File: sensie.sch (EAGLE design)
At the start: 26 parts, among them J2 BATT, Q1 MOSFET-PCHANNELSMD, Q2 MOSFET-NCHANNELBSS138, Q3 20MHz

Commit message: Routing cleanup 3.
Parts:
- removed JP1: USB-MICROB, SparkFun-Connectors:USB-MICROB
- added JP3: USB-MICROB, bafoontecha:USB-MICROB
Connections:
- removed net N$3: J2-2.S
- net GND: now also J2-2.S, JP3.GND; no longer JP1.GND
- net N$14: now also JP3.D+; no longer JP1.D+
- net N$15: now also JP3.D-; no longer JP1.D-
- net VIN_USB: now also JP3.VBUS; no longer JP1.VBUS
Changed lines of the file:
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@@
 <part name="GND7" library="supply1" deviceset="GND" device=""/>
 <part name="GND9" library="supply1" deviceset="GND" device=""/>
-<part name="JP1" library="SparkFun-Connectors" deviceset="USB" device="-MICROB"/>
 <part name="GND11" library="supply1" deviceset="GND" device=""/>
 <part name="Q2" library="SparkFun-DiscreteSemi" deviceset="MOSFET-NCHANNEL" device="BSS138"/>
 <part name="GND12" library="supply1" deviceset="GND" device=""/>
 <part name="JP2" library="SparkFun-Connectors" deviceset="M07" device=""/>
+<part name="JP3" library="bafoontecha" deviceset="USB" device="-MICROB"/>
 </parts>
 <sheets>
@@
 <instance part="GND7" gate="1" x="53.34" y="35.56"/>
 <instance part="GND9" gate="1" x="177.546" y="147.32"/>
-<instance part="JP1" gate="G$1" x="182.626" y="153.67"/>
 <instance part="GND11" gate="1" x="358.14" y="53.34"/>
 <instance part="Q2" gate="G$1" x="332.74" y="45.72"/>
 <instance part="GND12" gate="1" x="332.74" y="35.56"/>
 <instance part="JP2" gate="G$1" x="279.4" y="38.1" rot="R180"/>
+<instance part="JP3" gate="G$1" x="183.134" y="153.67"/>
 </instances>
 <busses>
@@
 <wire x1="274.32" y1="63.5" x2="264.16" y2="63.5" width="0.1524" layer="91"/>
 <label x="264.16" y="63.5" size="1.778" layer="95"/>
+<junction x="274.32" y="63.5"/>
 </segment>
 <segment>
@@
 <wire x1="53.34" y1="43.18" x2="58.42" y2="43.18" width="0.1524" layer="91"/>
 <wire x1="53.34" y1="38.1" x2="53.34" y2="43.18" width="0.1524" layer="91"/>
-</segment>
-<segment>
-<pinref part="JP1" gate="G$1" pin="GND"/>
+<junction x="53.34" y="43.18"/>
+</segment>
+<segment>
 <pinref part="GND9" gate="1" pin="GND"/>
-<wire x1="180.086" y1="153.67" x2="177.546" y2="153.67" width="0.1524" layer="91"/>
+<wire x1="180.594" y1="153.67" x2="177.546" y2="153.67" width="0.1524" layer="91"/>
 <wire x1="177.546" y1="153.67" x2="177.546" y2="149.86" width="0.1524" layer="91"/>
+<pinref part="JP3" gate="G$1" pin="GND"/>
+<junction x="180.594" y="153.67"/>
 </segment>
 <segment>
@@
 <pinref part="GND11" gate="1" pin="GND"/>
 <wire x1="358.14" y1="58.42" x2="358.14" y2="55.88" width="0.1524" layer="91"/>
+<junction x="358.14" y="58.42"/>
+<junction x="358.14" y="60.96"/>
+<junction x="358.14" y="63.5"/>
+<junction x="358.14" y="66.04"/>
+<junction x="358.14" y="71.12"/>
+<junction x="358.14" y="68.58"/>
+<junction x="358.14" y="73.66"/>
 </segment>
 <segment>
@@
 <pinref part="GND12" gate="1" pin="GND"/>
 <wire x1="332.74" y1="40.64" x2="332.74" y2="38.1" width="0.1524" layer="91"/>
+<junction x="332.74" y="40.64"/>
+<junction x="332.74" y="38.1"/>
 </segment>
 <segment>
@@
 <wire x1="312.42" y1="106.68" x2="312.42" y2="104.14" width="0.1524" layer="91"/>
 <wire x1="312.42" y1="104.14" x2="314.96" y2="104.14" width="0.1524" layer="91"/>
+<junction x="314.96" y="104.14"/>
+<junction x="312.42" y="106.68"/>
 </segment>
 <segment>
@@
 <wire x1="274.32" y1="76.2" x2="264.16" y2="76.2" width="0.1524" layer="91"/>
 <label x="264.16" y="76.2" size="1.778" layer="95"/>
+<junction x="274.32" y="76.2"/>
+</segment>
+<segment>
+<pinref part="J2" gate="-2" pin="S"/>
+<wire x1="287.02" y1="223.52" x2="287.02" y2="222.25" width="0.1524" layer="91"/>
+<junction x="287.02" y="223.52"/>
+<pinref part="GND2" gate="1" pin="GND"/>
+<junction x="287.02" y="222.25"/>
+<wire x1="287.02" y1="222.25" x2="287.02" y2="221.996" width="0.1524" layer="91"/>
 </segment>
 </net>
@@
 </segment>
 <segment>
-<wire x1="180.086" y1="156.21" x2="170.942" y2="156.21" width="0.1524" layer="91"/>
+<wire x1="180.594" y1="156.21" x2="170.942" y2="156.21" width="0.1524" layer="91"/>
 <label x="162.56" y="156.464" size="1.778" layer="95"/>
-<pinref part="JP1" gate="G$1" pin="VBUS"/>
+<pinref part="JP3" gate="G$1" pin="VBUS"/>
+<junction x="180.594" y="156.21"/>
 </segment>
 </net>
@@
 <net name="N$14" class="0">
 <segment>
-<wire x1="143.51" y1="161.29" x2="180.086" y2="161.29" width="0.1524" layer="91"/>
+<wire x1="143.51" y1="161.29" x2="180.594" y2="161.29" width="0.1524" layer="91"/>
 <pinref part="U$3" gate="G$1" pin="RC5/D+"/>
-<pinref part="JP1" gate="G$1" pin="D+"/>
+<pinref part="JP3" gate="G$1" pin="D+"/>
+<junction x="180.594" y="161.29"/>
 </segment>
 </net>
 <net name="N$15" class="0">
 <segment>
-<wire x1="180.086" y1="158.75" x2="143.51" y2="158.75" width="0.1524" layer="91"/>
+<wire x1="180.594" y1="158.75" x2="143.51" y2="158.75" width="0.1524" layer="91"/>
 <pinref part="U$3" gate="G$1" pin="RC4/D-"/>
-<pinref part="JP1" gate="G$1" pin="D-"/>
+<pinref part="JP3" gate="G$1" pin="D-"/>
+<junction x="180.594" y="158.75"/>
 </segment>
 </net>
@@
 <pinref part="IC1" gate="G$1" pin="OUT"/>
 <wire x1="359.41" y1="210.82" x2="375.92" y2="210.82" width="0.1524" layer="91"/>
+<junction x="375.92" y="210.82"/>
 </segment>
 <segment>
@@
 <wire x1="330.2" y1="104.14" x2="335.28" y2="104.14" width="0.1524" layer="91"/>
 <label x="332.74" y="104.14" size="1.778" layer="95"/>
+<junction x="330.2" y="104.14"/>
 </segment>
 <segment>
@@
 <label x="264.16" y="66.04" size="1.778" layer="95"/>
 <label x="264.16" y="66.04" size="1.778" layer="95"/>
+<junction x="274.32" y="66.04"/>
 </segment>
 <segment>
@@
 <pinref part="Q2" gate="G$1" pin="D"/>
 <wire x1="332.74" y1="58.42" x2="332.74" y2="50.8" width="0.1524" layer="91"/>
+<junction x="332.74" y="58.42"/>
+<junction x="332.74" y="60.96"/>
+<junction x="332.74" y="63.5"/>
+<junction x="332.74" y="66.04"/>
+<junction x="332.74" y="68.58"/>
+<junction x="332.74" y="71.12"/>
+<junction x="332.74" y="73.66"/>
+<junction x="332.74" y="50.8"/>
 </segment>
 <segment>
@@
 <wire x1="274.32" y1="88.9" x2="264.16" y2="88.9" width="0.1524" layer="91"/>
 <label x="264.16" y="88.9" size="1.778" layer="95"/>
+<junction x="274.32" y="88.9"/>
 </segment>
 </net>
@@
 <label x="264.16" y="40.64" size="1.778" layer="95"/>
 <pinref part="JP2" gate="G$1" pin="2"/>
+<junction x="274.32" y="40.64"/>
 </segment>
 </net>
@@
 <label x="264.16" y="38.1" size="1.778" layer="95"/>
 <pinref part="JP2" gate="G$1" pin="3"/>
+<junction x="274.32" y="38.1"/>
 </segment>
 </net>
@@
 <label x="264.16" y="35.56" size="1.778" layer="95"/>
 <pinref part="JP2" gate="G$1" pin="4"/>
+<junction x="274.32" y="35.56"/>
 </segment>
 </net>
@@
 <label x="264.16" y="33.02" size="1.778" layer="95"/>
 <pinref part="JP2" gate="G$1" pin="5"/>
-</segment>
-</net>
-<net name="N$3" class="0">
-<segment>
-<pinref part="J2" gate="-2" pin="S"/>
-<wire x1="287.02" y1="223.52" x2="287.02" y2="221.996" width="0.1524" layer="91"/>
+<junction x="274.32" y="33.02"/>
 </segment>
 </net>
@@
 <wire x1="330.2" y1="101.6" x2="335.28" y2="101.6" width="0.1524" layer="91"/>
 <label x="332.74" y="101.6" size="1.778" layer="95"/>
+<junction x="330.2" y="101.6"/>
 </segment>
 <segment>
@@
 <wire x1="330.2" y1="99.06" x2="335.28" y2="99.06" width="0.1524" layer="91"/>
 <label x="332.74" y="99.06" size="1.778" layer="95"/>
+<junction x="330.2" y="99.06"/>
 </segment>
 <segment>
@@
 <wire x1="274.32" y1="60.96" x2="264.16" y2="60.96" width="0.1524" layer="91"/>
 <label x="254" y="60.96" size="1.778" layer="95"/>
+<junction x="274.32" y="60.96"/>
 </segment>
 </net>
@@
 <wire x1="330.2" y1="96.52" x2="335.28" y2="96.52" width="0.1524" layer="91"/>
 <label x="332.74" y="96.52" size="1.778" layer="95"/>
+<junction x="330.2" y="96.52"/>
 </segment>
 <segment>
@@
 <wire x1="314.96" y1="101.6" x2="310.642" y2="101.6" width="0.1524" layer="91"/>
 <label x="298.45" y="101.854" size="1.778" layer="95"/>
+<junction x="314.96" y="101.6"/>
 </segment>
 <segment>
@@
 <wire x1="314.96" y1="99.06" x2="310.642" y2="99.06" width="0.1524" layer="91"/>
 <label x="298.45" y="99.314" size="1.778" layer="95"/>
+<junction x="314.96" y="99.06"/>
 </segment>
 <segment>
@@
 <wire x1="274.32" y1="81.28" x2="264.16" y2="81.28" width="0.1524" layer="91"/>
 <label x="264.16" y="81.28" size="1.778" layer="95"/>
+<junction x="274.32" y="81.28"/>
 </segment>
 </net>
@@
 <wire x1="314.96" y1="96.52" x2="310.642" y2="96.52" width="0.1524" layer="91"/>
 <label x="298.45" y="96.774" size="1.778" layer="95"/>
+<junction x="314.96" y="96.52"/>
 </segment>
 <segment>
@@
 <wire x1="274.32" y1="78.74" x2="264.16" y2="78.74" width="0.1524" layer="91"/>
 <label x="264.16" y="78.74" size="1.778" layer="95"/>
+<junction x="274.32" y="78.74"/>
 </segment>
 </net>
@@
 <wire x1="274.32" y1="83.82" x2="264.16" y2="83.82" width="0.1524" layer="91"/>
 <label x="264.16" y="83.82" size="1.778" layer="95"/>
+<junction x="274.32" y="83.82"/>
 </segment>
 </net>
@@
 <wire x1="274.32" y1="86.36" x2="264.16" y2="86.36" width="0.1524" layer="91"/>
 <label x="264.16" y="86.36" size="1.778" layer="95"/>
+<junction x="274.32" y="86.36"/>
 </segment>
 </net>
@@
 <wire x1="325.12" y1="45.72" x2="317.5" y2="45.72" width="0.1524" layer="91"/>
 <label x="306.832" y="45.72" size="1.778" layer="95"/>
+<junction x="325.12" y="45.72"/>
 </segment>
 </net>
@@
 <label x="264.16" y="30.48" size="1.778" layer="95"/>
 <pinref part="JP2" gate="G$1" pin="6"/>
+<junction x="274.32" y="30.48"/>
 </segment>
 </net>
@@
 <label x="264.16" y="27.94" size="1.778" layer="95"/>
 <pinref part="JP2" gate="G$1" pin="7"/>
+<junction x="274.32" y="27.94"/>
 </segment>
 </net>
@@
 <wire x1="274.32" y1="58.42" x2="264.16" y2="58.42" width="0.1524" layer="91"/>
 <label x="254" y="58.42" size="1.778" layer="95"/>
+<junction x="274.32" y="58.42"/>
 </segment>
 <segment>
@@
 <pinref part="R1" gate="G$1" pin="1"/>
 <wire x1="58.42" y1="55.88" x2="58.42" y2="63.5" width="0.1524" layer="91"/>
+<junction x="58.42" y="55.88"/>
 </segment>
 </net>
@@
 <wire x1="48.26" y1="55.88" x2="48.26" y2="76.2" width="0.1524" layer="91"/>
 <label x="48.26" y="76.2" size="1.778" layer="95"/>
+<junction x="48.26" y="55.88"/>
 </segment>
 <segment>
@@
 <wire x1="274.32" y1="43.18" x2="263.906" y2="43.18" width="0.1524" layer="91"/>
 <label x="264.16" y="43.18" size="1.778" layer="95"/>
-</segment>
-<segment>
+<junction x="274.32" y="43.18"/>
+</segment>
+<segment>

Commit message: About to do ground pours.
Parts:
- removed R13: 10k, SparkFun:RESISTOR
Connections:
- net 3.3V: now also SENSOR.6; no longer R13.2, SENSOR.1
- net GND: now also SENSOR.1; no longer SENSOR.6
- net VPP: no longer R13.1
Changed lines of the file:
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@@
 <part name="C6" library="SparkFun" deviceset="CAP" device="SMD" value="10uF"/>
 <part name="GND19" library="SparkFun" deviceset="GND" device=""/>
-<part name="GND24" library="SparkFun" deviceset="GND" device=""/>
-<part name="R13" library="SparkFun" deviceset="RESISTOR" device="" value="10k"/>
-<part name="P+4" library="SparkFun" deviceset="3.3V" device=""/>
 <part name="GND2" library="SparkFun" deviceset="GND" device=""/>
 <part name="GND3" library="supply1" deviceset="GND" device=""/>
@@
 <instance part="C6" gate="G$1" x="375.92" y="203.2"/>
 <instance part="GND19" gate="1" x="375.92" y="198.12"/>
-<instance part="GND24" gate="1" x="58.42" y="205.74"/>
-<instance part="R13" gate="G$1" x="58.42" y="226.06" rot="R90"/>
-<instance part="P+4" gate="G$1" x="58.42" y="231.14"/>
 <instance part="GND2" gate="1" x="287.02" y="219.71"/>
 <instance part="GND3" gate="1" x="312.42" y="109.22" rot="R180"/>
@@
 </segment>
 <segment>
-<wire x1="213.36" y1="182.88" x2="205.74" y2="182.88" width="0.1524" layer="91"/>
+<wire x1="217.17" y1="182.88" x2="205.74" y2="182.88" width="0.1524" layer="91"/>
 <label x="205.74" y="182.88" size="1.778" layer="95"/>
 </segment>
@@
 </segment>
 <segment>
-<pinref part="SENSOR" gate="G$1" pin="6"/>
-<wire x1="274.32" y1="76.2" x2="264.16" y2="76.2" width="0.1524" layer="91"/>
-<label x="264.16" y="76.2" size="1.778" layer="95"/>
-<junction x="274.32" y="76.2"/>
-</segment>
-<segment>
 <pinref part="J2" gate="-2" pin="S"/>
 <wire x1="287.02" y1="223.52" x2="287.02" y2="222.25" width="0.1524" layer="91"/>
@@
 <junction x="287.02" y="222.25"/>
 <wire x1="287.02" y1="222.25" x2="287.02" y2="221.996" width="0.1524" layer="91"/>
+</segment>
+<segment>
+<pinref part="SENSOR" gate="G$1" pin="1"/>
+<wire x1="274.32" y1="88.9" x2="264.16" y2="88.9" width="0.1524" layer="91"/>
+<label x="264.16" y="88.9" size="1.778" layer="95"/>
+<junction x="274.32" y="88.9"/>
 </segment>
 </net>
@@
 <net name="VPP" class="0">
 <segment>
-<wire x1="213.36" y1="177.8" x2="205.74" y2="177.8" width="0.1524" layer="91"/>
+<wire x1="217.17" y1="177.8" x2="205.74" y2="177.8" width="0.1524" layer="91"/>
 <label x="205.74" y="177.8" size="1.778" layer="95"/>
 </segment>
@@
 <label x="90.17" y="191.77" size="1.778" layer="95"/>
 <pinref part="U$3" gate="G$1" pin="MCLR/VPP"/>
-</segment>
-<segment>
-<wire x1="58.42" y1="220.98" x2="58.42" y2="219.71" width="0.1524" layer="91"/>
-<wire x1="58.42" y1="219.71" x2="58.42" y2="218.44" width="0.1524" layer="91"/>
-<wire x1="58.42" y1="219.71" x2="66.04" y2="219.71" width="0.1524" layer="91"/>
-<junction x="58.42" y="219.71"/>
-<label x="60.96" y="219.71" size="1.778" layer="95"/>
-<pinref part="R13" gate="G$1" pin="1"/>
 </segment>
 </net>
@@
 </segment>
 <segment>
-<wire x1="213.36" y1="180.34" x2="205.74" y2="180.34" width="0.1524" layer="91"/>
+<wire x1="217.17" y1="180.34" x2="205.74" y2="180.34" width="0.1524" layer="91"/>
 <label x="205.74" y="180.34" size="1.778" layer="95"/>
-</segment>
-<segment>
-<pinref part="R13" gate="G$1" pin="2"/>
-<pinref part="P+4" gate="G$1" pin="3.3V"/>
 </segment>
 <segment>
@@
 </segment>
 <segment>
-<pinref part="SENSOR" gate="G$1" pin="1"/>
-<wire x1="274.32" y1="88.9" x2="264.16" y2="88.9" width="0.1524" layer="91"/>
-<label x="264.16" y="88.9" size="1.778" layer="95"/>
-<junction x="274.32" y="88.9"/>
+<pinref part="SENSOR" gate="G$1" pin="6"/>
+<wire x1="274.32" y1="76.2" x2="264.16" y2="76.2" width="0.1524" layer="91"/>
+<label x="264.16" y="76.2" size="1.778" layer="95"/>
+<junction x="274.32" y="76.2"/>
 </segment>
 </net>
@@
 </segment>
 </net>
-<net name="LCD_DB5" class="0">
-<segment>
-<wire x1="213.36" y1="190.5" x2="205.74" y2="190.5" width="0.1524" layer="91"/>
-<label x="205.74" y="190.5" size="1.778" layer="95"/>
-</segment>
-</net>
-<net name="LCD_DB6" class="0">
-<segment>
-<wire x1="213.36" y1="187.96" x2="205.74" y2="187.96" width="0.1524" layer="91"/>
-<label x="205.74" y="187.96" size="1.778" layer="95"/>
-</segment>
-</net>
-<net name="LCD_DB7" class="0">
-<segment>
-<wire x1="213.36" y1="185.42" x2="205.74" y2="185.42" width="0.1524" layer="91"/>
-<label x="205.74" y="185.42" size="1.778" layer="95"/>
-</segment>
-</net>
 <net name="AN3" class="0">
 <segment>
@@
 <junction x="274.32" y="83.82"/>
 </segment>
+<segment>
+<wire x1="217.17" y1="190.5" x2="205.74" y2="190.5" width="0.1524" layer="91"/>
+<label x="205.74" y="190.5" size="1.778" layer="95"/>
+</segment>
 </net>
 <net name="BMP_EOC" class="0">
@@
 <junction x="274.32" y="86.36"/>
 </segment>
+<segment>
+<wire x1="217.17" y1="187.96" x2="205.74" y2="187.96" width="0.1524" layer="91"/>
+<label x="205.74" y="187.96" size="1.778" layer="95"/>
+</segment>
 </net>
 <net name="ANALOG_ENABLE" class="0">
@@
 <junction x="325.12" y="45.72"/>
 </segment>
-</net>
+<segment>
+<wire x1="217.17" y1="185.42" x2="205.74" y2="185.42" width="0.1524" layer="91"/>
+<label x="205.74" y="185.42" size="1.778" layer="95"/>
+</segment>
+</net>

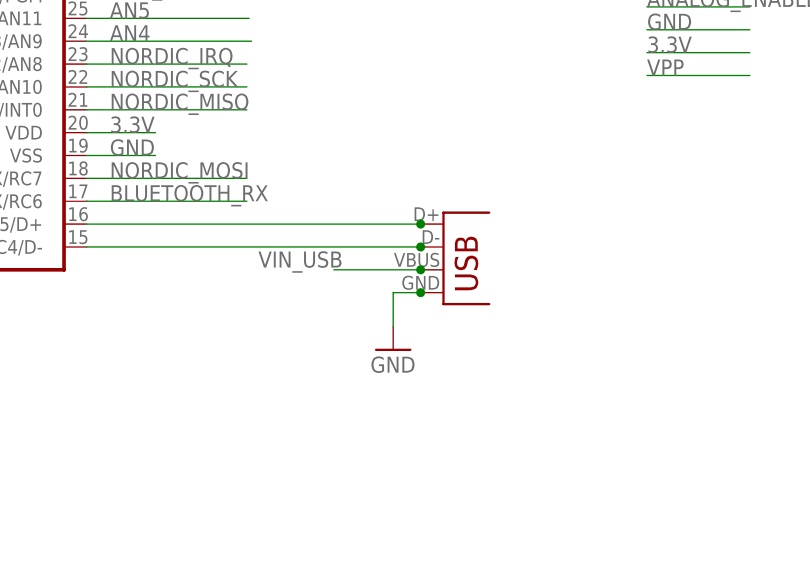
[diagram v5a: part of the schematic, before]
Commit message: Rerouting Nordic Power.
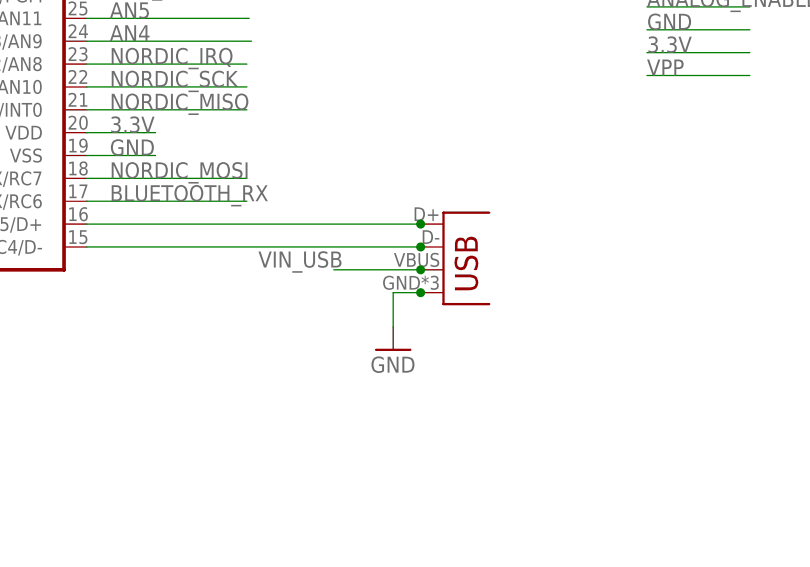
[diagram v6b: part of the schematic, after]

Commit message: Sent to OshPark.
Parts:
- added POW!: (no value), SparkFun-LED:LED0603
- added R2, R3, R4: (no value), SparkFun-Passives:RESISTOR0603-RES
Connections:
- new net N$3: POW!.A, R2.1
- net 3.3V: now also R3.2, R4.2
- net AN0: now also R4.1
- net COUNTER: now also R3.1
- net GND: now also POW!.C
- net VIN_USB: now also R2.2
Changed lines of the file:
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@@
 <part name="JP2" library="SparkFun-Connectors" deviceset="M07" device=""/>
 <part name="JP3" library="bafoontecha" deviceset="USB" device="-MICROB"/>
+<part name="R2" library="SparkFun-Passives" deviceset="RESISTOR" device="0603-RES"/>
+<part name="POW!" library="SparkFun-LED" deviceset="LED" device="0603"/>
+<part name="GND4" library="supply1" deviceset="GND" device=""/>
+<part name="R3" library="SparkFun-Passives" deviceset="RESISTOR" device="0603-RES"/>
+<part name="R4" library="SparkFun-Passives" deviceset="RESISTOR" device="0603-RES"/>
 </parts>
 <sheets>
@@
 <instance part="JP2" gate="G$1" x="279.4" y="38.1" rot="R180"/>
 <instance part="JP3" gate="G$1" x="183.134" y="153.67"/>
+<instance part="R2" gate="G$1" x="154.94" y="68.58" rot="R90"/>
+<instance part="POW!" gate="G$1" x="154.94" y="60.96"/>
+<instance part="GND4" gate="1" x="154.94" y="53.34"/>
+<instance part="R3" gate="G$1" x="190.5" y="83.82" rot="R180"/>
+<instance part="R4" gate="G$1" x="190.5" y="76.2" rot="R180"/>
 </instances>
 <busses>
@@
 <junction x="274.32" y="88.9"/>
 </segment>
+<segment>
+<pinref part="POW!" gate="G$1" pin="C"/>
+<pinref part="GND4" gate="1" pin="GND"/>
+</segment>
 </net>
 <net name="VIN_USB" class="0">
@@
 <pinref part="JP3" gate="G$1" pin="VBUS"/>
 <junction x="180.594" y="156.21"/>
+</segment>
+<segment>
+<pinref part="R2" gate="G$1" pin="2"/>
+<wire x1="154.94" y1="73.66" x2="154.94" y2="78.74" width="0.1524" layer="91"/>
+<label x="154.94" y="78.74" size="1.778" layer="95"/>
 </segment>
 </net>
@@
 <junction x="274.32" y="76.2"/>
 </segment>
+<segment>
+<pinref part="R3" gate="G$1" pin="2"/>
+<wire x1="185.42" y1="83.82" x2="175.26" y2="83.82" width="0.1524" layer="91"/>
+<label x="175.26" y="83.82" size="1.778" layer="95"/>
+</segment>
+<segment>
+<pinref part="R4" gate="G$1" pin="2"/>
+<wire x1="185.42" y1="76.2" x2="175.26" y2="76.2" width="0.1524" layer="91"/>
+<label x="175.26" y="76.2" size="1.778" layer="95"/>
+</segment>
 </net>
 <net name="N$10" class="0">
@@
 <junction x="274.32" y="40.64"/>
 </segment>
+<segment>
+<pinref part="R4" gate="G$1" pin="1"/>
+<wire x1="195.58" y1="76.2" x2="205.74" y2="76.2" width="0.1524" layer="91"/>
+<label x="195.58" y="76.2" size="1.778" layer="95"/>
+</segment>
 </net>
 <net name="AN1" class="0">
@@
 <label x="89.916" y="179.07" size="1.778" layer="95"/>
 </segment>
-</net>
+<segment>
+<pinref part="R3" gate="G$1" pin="1"/>
+<wire x1="195.58" y1="83.82" x2="205.74" y2="83.82" width="0.1524" layer="91"/>
+<label x="195.58" y="83.82" size="1.778" layer="95"/>
+</segment>
+</net>
+<net name="N$3" class="0">
+<segment>
+<pinref part="R2" gate="G$1" pin="1"/>
+<pinref part="POW!" gate="G$1" pin="A"/>
+</segment>
+</net>
